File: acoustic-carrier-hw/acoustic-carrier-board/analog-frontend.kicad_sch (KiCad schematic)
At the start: 97 parts, among them J1001 BWU.FL-IPEX1, J1002 BWU.FL-IPEX1, J1003 BWU.FL-IPEX1, J1005 BWU.FL-IPEX1, J1006 BWU.FL-IPEX1, J1007 8P8C_Shielded, J1008 BWU.FL-IPEX1, J1009 BWU.FL-IPEX1, J1010 BWU.FL-IPEX1, U1001 MS9280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

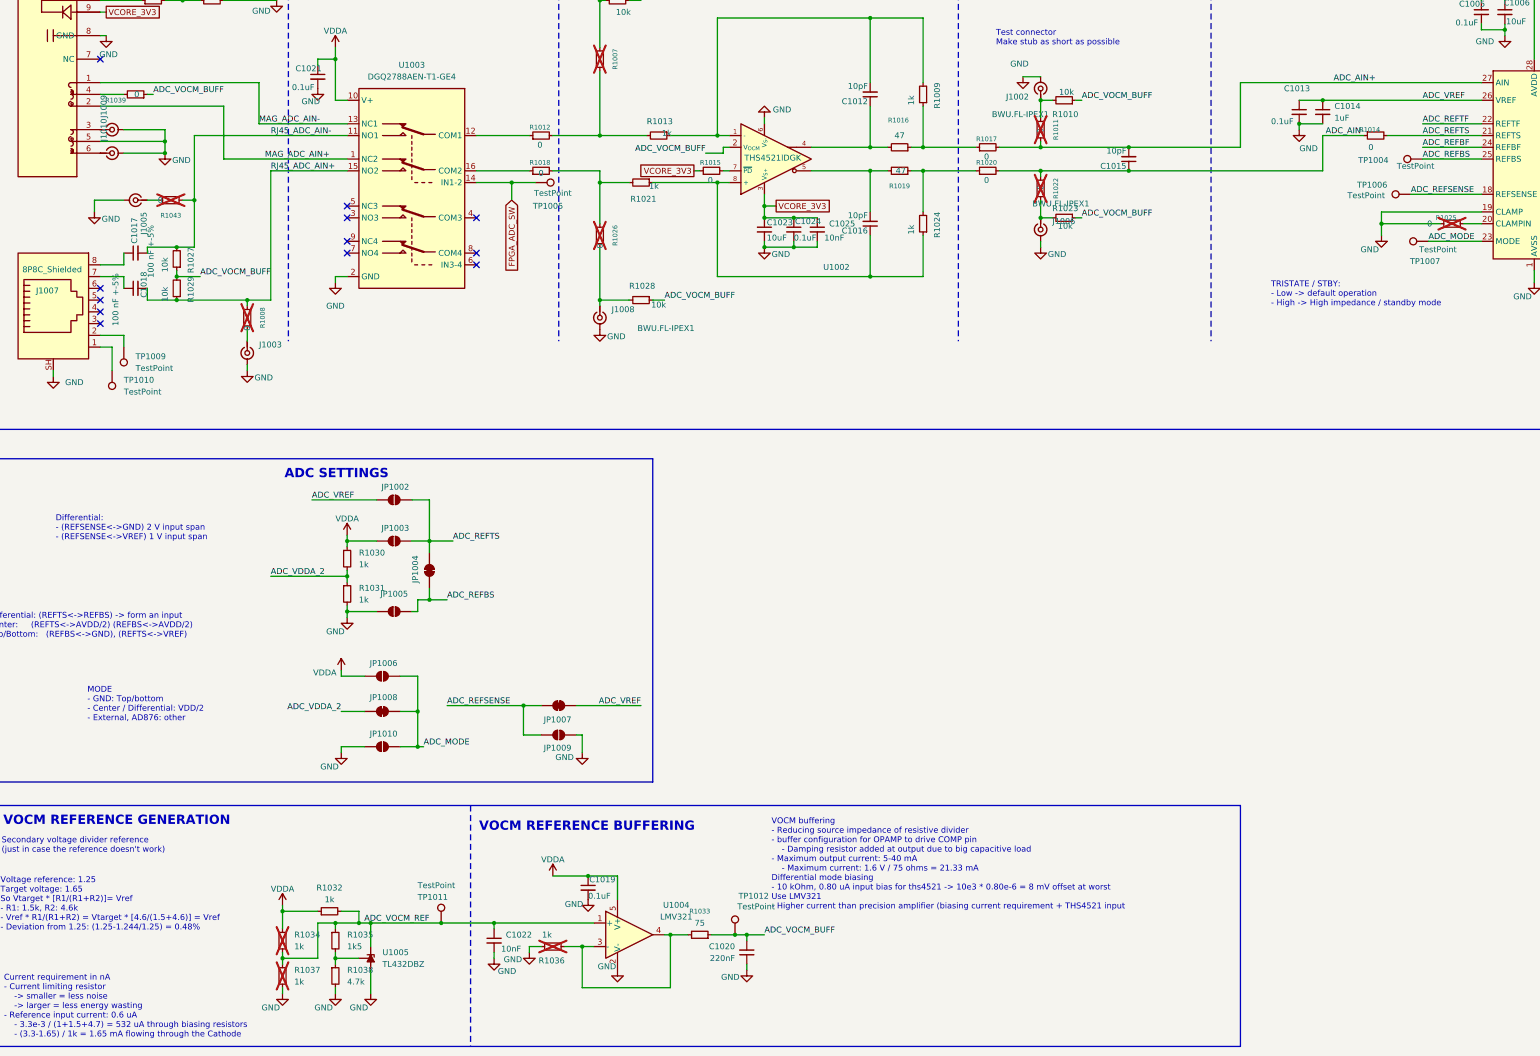
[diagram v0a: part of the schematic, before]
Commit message: [carrier] Added extra decoupling to ADC bias voltage
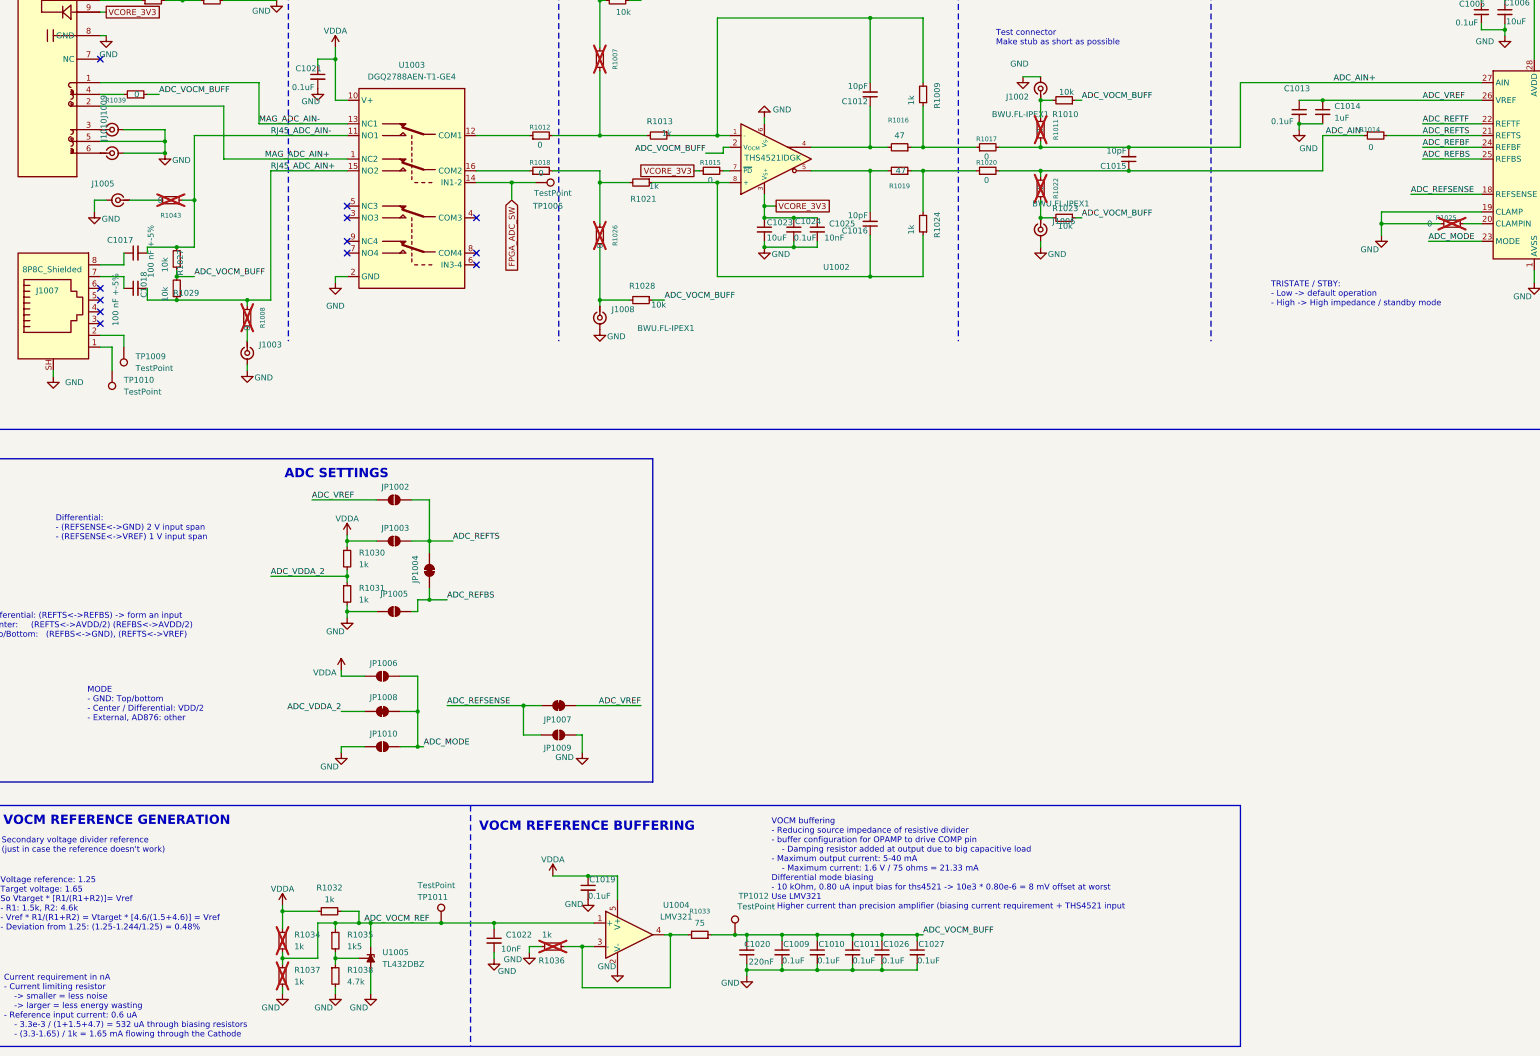
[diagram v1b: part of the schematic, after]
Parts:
- removed TP1004, TP1006, TP1007: TestPoint, TestPoint:TestPoint_Loop_D1.80mm_Drill1.0mm_Beaded, symbol Connector:TestPoint
- added C1009, C1010, C1011, C1026, C1027: 0.1uF, Capacitor_SMD:C_0201_0603Metric, symbol Device:C_Small
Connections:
- net ADC_VOCM_BUFF: now also C1009.1, C1010.1, C1011.1, C1026.1, C1027.1
- net GND: now also C1009.2, C1010.2, C1011.2, C1026.2, C1027.2
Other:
- moved on the sheet: J1005

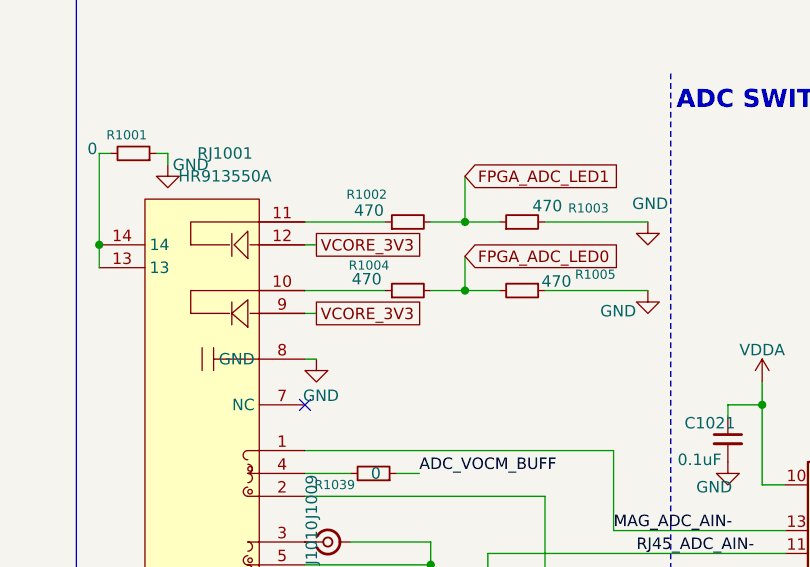
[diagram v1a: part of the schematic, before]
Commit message: [carrier] Added delayed startup + some traces (next) fix the errors inside the DDR3 routing somehow
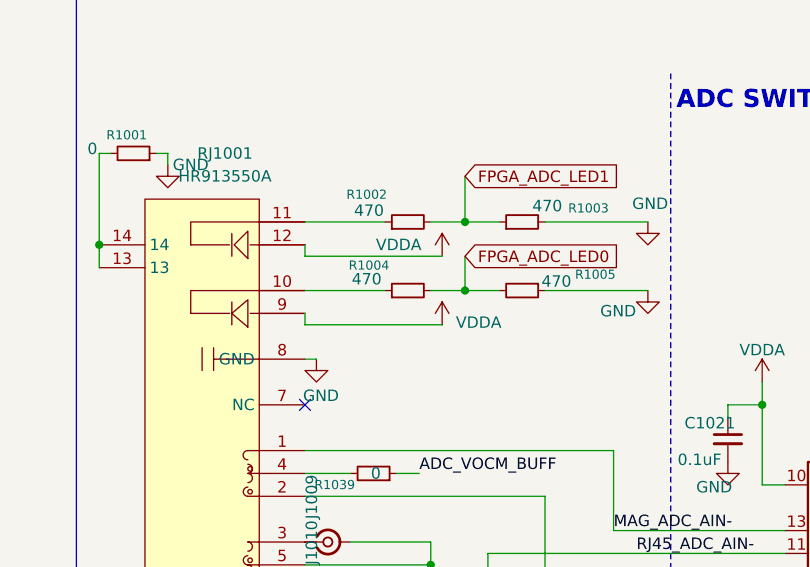
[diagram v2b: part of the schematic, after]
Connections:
- net VCORE_3V3: no longer RJ1001.12, RJ1001.9
- net VDDA: now also RJ1001.12, RJ1001.9
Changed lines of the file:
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@@
 	(wire
 		(pts
+			(xy 39.37 58.42) (xy 39.37 57.15)
+		)
+		(stroke
+			(width 0)
+			(type default)
+		)
+	)
+	(wire
+		(pts
 			(xy 92.71 179.07) (xy 92.71 180.34)
 		)
@@
 		)
 	)
+	(wire
+		(pts
+			(xy 39.37 50.8) (xy 39.37 49.53)
+		)
+		(stroke
+			(width 0)
+			(type default)
+		)
+	)
 	(bus
 		(pts
@@
 	(wire
 		(pts
-			(xy 39.37 57.15) (xy 40.64 57.15)
+			(xy 39.37 58.42) (xy 54.61 58.42)
+		)
+		(stroke
+			(width 0)
+			(type default)
+		)
+	)
+	(wire
+		(pts
+			(xy 39.37 50.8) (xy 54.61 50.8)
 		)
 		(stroke
@@
 	(wire
 		(pts
-			(xy 39.37 49.53) (xy 40.64 49.53)
-		)
-		(stroke
-			(width 0)
-			(type default)
-		)
-	)
-	(wire
-		(pts
 			(xy 92.71 186.69) (xy 99.06 186.69)
 		)
@@
 		)
 	)
-	(global_label "VCORE_3V3"
-		(shape passive)
-		(at 40.64 57.15 0)
-		(fields_autoplaced yes)
-		(effects
-			(font
-				(size 1.27 1.27)
-			)
-			(justify left)
-		)
-		(property "Intersheetrefs" "${INTERSHEET_REFS}"
-			(at 53.0972 57.15 0)
-			(effects
-				(font
-					(size 1.27 1.27)
-				)
-				(justify left)
-				(hide yes)
-			)
-		)
-	)
 	(global_label "FPGA_ADC_LED1"
 		(shape input)
@@
 		)
 	)
-	(global_label "VCORE_3V3"
-		(shape passive)
-		(at 40.64 49.53 0)
-		(fields_autoplaced yes)
-		(effects
-			(font
-				(size 1.27 1.27)
-			)
-			(justify left)
-		)
-		(property "Intersheetrefs" "${INTERSHEET_REFS}"
-			(at 53.0972 49.53 0)
-			(effects
-				(font
-					(size 1.27 1.27)
-				)
-				(justify left)
-				(hide yes)
-			)
-		)
-	)
 	(global_label "FPGA_ADC_SW"
 		(shape input)
@@
 	)
 	(symbol
+		(lib_id "power:VDDA")
+		(at 54.61 50.8 0)
+		(unit 1)
+		(exclude_from_sim no)
+		(in_bom yes)
+		(on_board yes)
+		(dnp no)
+		(property "Reference" "#PWR01019"
+			(at 54.61 54.61 0)
+			(effects
+				(font
+					(size 1.27 1.27)
+				)
+				(hide yes)
+			)
+		)
+		(property "Value" "VDDA"
+			(at 49.784 49.53 0)
+			(effects
+				(font
+					(size 1.27 1.27)
+				)
+			)
+		)
+		(property "Footprint" ""
+			(at 54.61 50.8 0)
+			(effects
+				(font
+					(size 1.27 1.27)
+				)
+				(hide yes)
+			)
+		)
+		(property "Datasheet" ""
+			(at 54.61 50.8 0)
+			(effects
+				(font
+					(size 1.27 1.27)
+				)
+				(hide yes)
+			)
+		)
+		(property "Description" "Power symbol creates a global label with name \"VDDA\""
+			(at 54.61 50.8 0)
+			(effects
+				(font
+					(size 1.27 1.27)
+				)
+				(hide yes)
+			)
+		)
+		(pin "1"
+		)
+		(instances
+			(project "acoustic-carrier-board"
+				(path "/25b015c9-ab13-4427-b72c-b6f348597100/94142f45-8b3d-48ce-ac4d-b9c7695832d7"
+					(reference "#PWR01019")
+					(unit 1)
+				)
+			)
+		)
+	)
+	(symbol
 		(lib_id "Device:C_Small")
 		(at 179.07 260.35 0)
@@
 					(unit 1)
 				)
+			)
+		)
+	)
+	(symbol
+		(lib_id "power:VDDA")
+		(at 54.61 58.42 0)
+		(unit 1)
+		(exclude_from_sim no)
+		(in_bom yes)
+		(on_board yes)
+		(dnp no)
+		(property "Reference" "#PWR01016"
+			(at 54.61 62.23 0)
+			(effects
+				(font
+					(size 1.27 1.27)
+				)
+				(hide yes)
+			)
+		)
+		(property "Value" "VDDA"
+			(at 58.674 58.166 0)
+			(effects
+				(font
+					(size 1.27 1.27)
+				)
+			)
+		)
+		(property "Footprint" ""
+			(at 54.61 58.42 0)
+			(effects
+				(font
+					(size 1.27 1.27)
+				)
+				(hide yes)
+			)
+		)
+		(property "Datasheet" ""
+			(at 54.61 58.42 0)
+			(effects
+				(font
+					(size 1.27 1.27)
+				)
+				(hide yes)
+			)
+		)
+		(property "Description" "Power symbol creates a global label with name \"VDDA\""
+			(at 54.61 58.42 0)
+			(effects
+				(font
+					(size 1.27 1.27)
+				)
+				(hide yes)
+			)
+		)
+		(pin "1"
+		)
+		(instances
+			(project ""
+				(path "/25b015c9-ab13-4427-b72c-b6f348597100/94142f45-8b3d-48ce-ac4d-b9c7695832d7"
+					(reference "#PWR01016")
+					(unit 1)
+				)

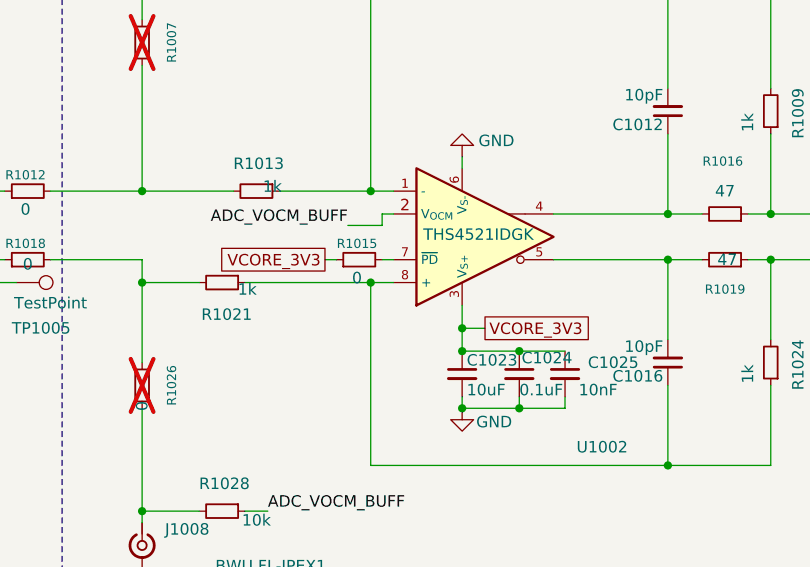
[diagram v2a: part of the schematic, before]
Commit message: [carrier] Corrected most of the DRC errors, a  few tens left + respacing DDR3-traces
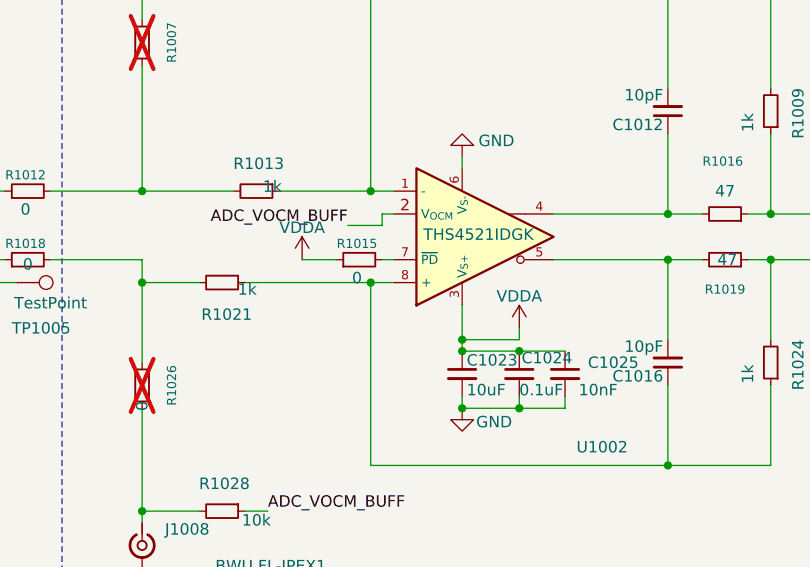
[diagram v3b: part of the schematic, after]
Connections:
- net VCORE_3V3: no longer C1023.1, C1024.1, C1025.1, R1015.1, U1002.3 (V_{S+})
- net VDDA: now also C1023.1, C1024.1, C1025.1, R1015.1, U1002.3 (V_{S+})
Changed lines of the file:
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@@
 	)
 	(junction
-		(at 182.88 99.06)
-		(diameter 0)
-		(color 0 0 0 0)
-	)
-	(junction
 		(at 147.32 119.38)
 		(diameter 0)
@@
 	)
 	(junction
+		(at 182.88 100.33)
+		(diameter 0)
+		(color 0 0 0 0)
+	)
+	(junction
 		(at 71.12 119.38)
 		(diameter 0)
@@
 	(wire
 		(pts
-			(xy 167.64 91.44) (xy 168.91 91.44)
+			(xy 165.1 91.44) (xy 168.91 91.44)
 		)
 		(stroke
@@
 	(wire
 		(pts
-			(xy 182.88 99.06) (xy 182.88 101.6)
-		)
-		(stroke
-			(width 0)
-			(type default)
-		)
-	)
-	(wire
-		(pts
 			(xy 55.88 113.03) (xy 55.88 114.3)
 		)
@@
 	(wire
 		(pts
+			(xy 182.88 100.33) (xy 182.88 101.6)
+		)
+		(stroke
+			(width 0)
+			(type default)
+		)
+	)
+	(wire
+		(pts
 			(xy 298.45 76.2) (xy 303.53 76.2)
 		)
@@
 	(wire
 		(pts
+			(xy 189.23 100.33) (xy 189.23 99.06)
+		)
+		(stroke
+			(width 0)
+			(type default)
+		)
+	)
+	(wire
+		(pts
 			(xy 173.99 91.44) (xy 175.26 91.44)
 		)
@@
 	(wire
 		(pts
+			(xy 182.88 96.52) (xy 182.88 100.33)
+		)
+		(stroke
+			(width 0)
+			(type default)
+		)
+	)
+	(wire
+		(pts
 			(xy 214.63 91.44) (xy 217.17 91.44)
 		)
@@
 	(wire
 		(pts
-			(xy 182.88 99.06) (xy 182.88 96.52)
-		)
-		(stroke
-			(width 0)
-			(type default)
-		)
-	)
-	(wire
-		(pts
 			(xy 303.53 83.82) (xy 312.42 83.82)
 		)
@@
 	(wire
 		(pts
-			(xy 185.42 99.06) (xy 182.88 99.06)
+			(xy 189.23 100.33) (xy 182.88 100.33)
 		)
 		(stroke
@@
 		)
 	)
-	(global_label "VCORE_3V3"
-		(shape passive)
-		(at 167.64 91.44 180)
-		(fields_autoplaced yes)
-		(effects
-			(font
-				(size 1.27 1.27)
-			)
-			(justify right)
-		)
-		(property "Intersheetrefs" "${INTERSHEET_REFS}"
-			(at 155.1828 91.44 0)
-			(effects
-				(font
-					(size 1.27 1.27)
-				)
-				(justify right)
-				(hide yes)
-			)
-		)
-	)
-	(global_label "VCORE_3V3"
-		(shape passive)
-		(at 185.42 99.06 0)
-		(fields_autoplaced yes)
-		(effects
-			(font
-				(size 1.27 1.27)
-			)
-			(justify left)
-		)
-		(property "Intersheetrefs" "${INTERSHEET_REFS}"
-			(at 197.8772 99.06 0)
-			(effects
-				(font
-					(size 1.27 1.27)
-				)
-				(justify left)
-				(hide yes)
-			)
-		)
-	)
 	(hierarchical_label "ADC{FPGA_ADC}"
 		(shape bidirectional)
@@
 	)
 	(symbol
+		(lib_id "power:VDDA")
+		(at 189.23 99.06 0)
+		(unit 1)
+		(exclude_from_sim no)
+		(in_bom yes)
+		(on_board yes)
+		(dnp no)
+		(property "Reference" "#PWR01020"
+			(at 189.23 102.87 0)
+			(effects
+				(font
+					(size 1.27 1.27)
+				)
+				(hide yes)
+			)
+		)
+		(property "Value" "VDDA"
+			(at 189.23 95.504 0)
+			(effects
+				(font
+					(size 1.27 1.27)
+				)
+			)
+		)
+		(property "Footprint" ""
+			(at 189.23 99.06 0)
+			(effects
+				(font
+					(size 1.27 1.27)
+				)
+				(hide yes)
+			)
+		)
+		(property "Datasheet" ""
+			(at 189.23 99.06 0)
+			(effects
+				(font
+					(size 1.27 1.27)
+				)
+				(hide yes)
+			)
+		)
+		(property "Description" "Power symbol creates a global label with name \"VDDA\""
+			(at 189.23 99.06 0)
+			(effects
+				(font
+					(size 1.27 1.27)
+				)
+				(hide yes)
+			)
+		)
+		(pin "1"
+		)
+		(instances
+			(project "acoustic-carrier-board"
+				(path "/25b015c9-ab13-4427-b72c-b6f348597100/94142f45-8b3d-48ce-ac4d-b9c7695832d7"
+					(reference "#PWR01020")
+					(unit 1)
+				)
+			)
+		)
+	)
+	(symbol
 		(lib_id "Device:C_Small")
 		(at 215.9 260.35 0)
@@
 					(unit 1)
 				)
+			)
+		)
+	)
+	(symbol
+		(lib_id "power:VDDA")
+		(at 165.1 91.44 0)
+		(unit 1)
+		(exclude_from_sim no)
+		(in_bom yes)
+		(on_board yes)
+		(dnp no)
+		(property "Reference" "#PWR01046"
+			(at 165.1 95.25 0)
+			(effects
+				(font
+					(size 1.27 1.27)
+				)
+				(hide yes)
+			)
+		)
+		(property "Value" "VDDA"
+			(at 165.1 87.884 0)
+			(effects
+				(font
+					(size 1.27 1.27)
+				)
+			)
+		)
+		(property "Footprint" ""
+			(at 165.1 91.44 0)
+			(effects
+				(font
+					(size 1.27 1.27)
+				)
+				(hide yes)
+			)
+		)
+		(property "Datasheet" ""
+			(at 165.1 91.44 0)
+			(effects
+				(font
+					(size 1.27 1.27)
+				)
+				(hide yes)
+			)
+		)
+		(property "Description" "Power symbol creates a global label with name \"VDDA\""
+			(at 165.1 91.44 0)
+			(effects
+				(font
+					(size 1.27 1.27)
+				)
+				(hide yes)
+			)
+		)
+		(pin "1"
+		)
+		(instances
+			(project "acoustic-carrier-board"
+				(path "/25b015c9-ab13-4427-b72c-b6f348597100/94142f45-8b3d-48ce-ac4d-b9c7695832d7"
+					(reference "#PWR01046")
+					(unit 1)
+				)
